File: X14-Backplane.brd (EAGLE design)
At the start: 88.9 x 139.7 mm, 34 parts, among them J2 PXC-PTSM-04-RA-1778641, J3 PXC-8-RA-1778683, J8 PXC-8-RA-1778683

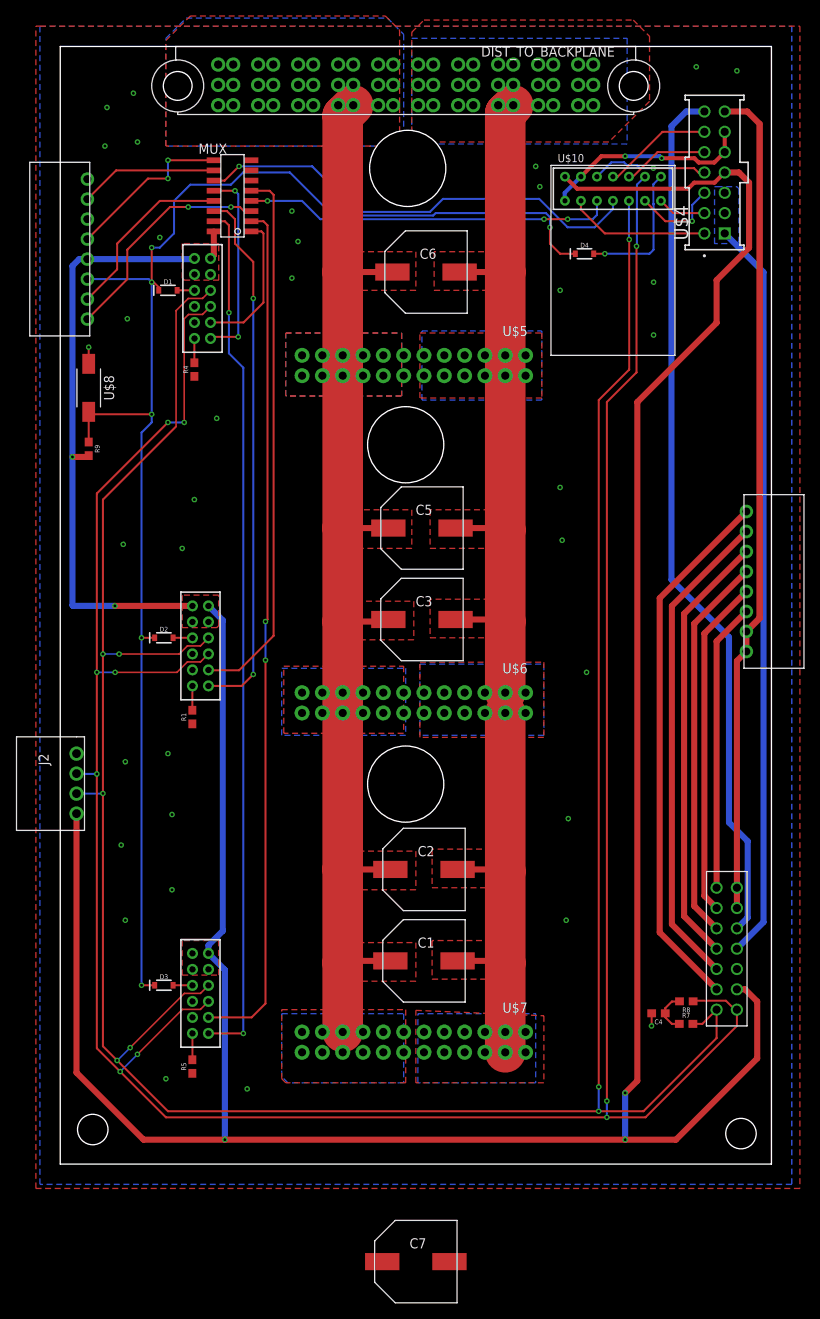
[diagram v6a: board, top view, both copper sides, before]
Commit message: todo: new cap, silkscreen
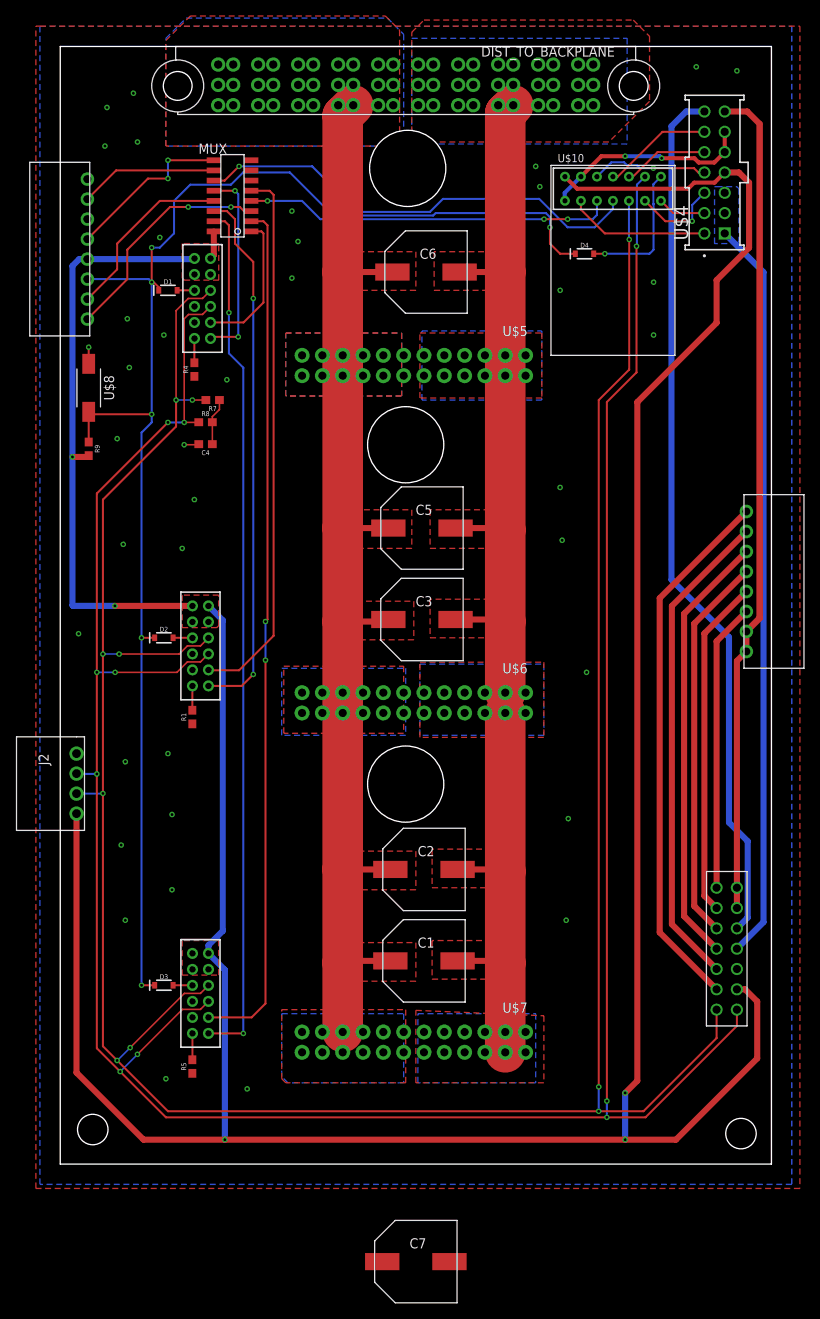
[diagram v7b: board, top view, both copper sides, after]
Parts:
- moved R7 97.9 mm to (19.1, 95.5), turned to 180 degrees
- moved R8 94.1 mm to (18.2, 92.7), turned to 0 degrees
- moved C4 90.9 mm to (18.2, 90.0)
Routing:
- net CAN_L: track 348.8 -> 344.7 mm
- net N$3: track 5.37 -> 5.88 mm
- net GND_L: track 30.0 -> 30.2 mm, vias 37 -> 41
- net CAN_H: track 340.2 -> 340.3 mm, vias 8 -> 10
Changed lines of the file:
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@@
 </autorouter>
 <elements>
-<element name="C4" library="SparkFun-Capacitors" library_urn="urn:adsk.eagle:library:510" package="0603" package3d_urn="urn:adsk.eagle:package:37414/1" value=".1uF" x="74.7776" y="18.8468" smashed="yes" rot="R180">
-<attribute name="NAME" x="74.7776" y="18.0848" size="0.6096" layer="25" font="vector" ratio="20" rot="R180" align="bottom-center"/>
-<attribute name="PROD_ID" value="CAP-00867" x="-20.4724" y="199.1868" size="1.778" layer="27" rot="R180" display="off"/>
-<attribute name="VALUE" x="74.7776" y="19.6088" size="0.6096" layer="27" font="vector" ratio="20" rot="R180" align="top-center"/>
+<element name="C4" library="SparkFun-Capacitors" library_urn="urn:adsk.eagle:library:510" package="0603" package3d_urn="urn:adsk.eagle:package:37414/1" value=".1uF" x="18.161" y="89.9922" smashed="yes" rot="R180">
+<attribute name="NAME" x="18.161" y="89.2302" size="0.6096" layer="25" font="vector" ratio="20" rot="R180" align="bottom-center"/>
+<attribute name="PROD_ID" value="CAP-00867" x="-77.089" y="270.3322" size="1.778" layer="27" rot="R180" display="off"/>
+<attribute name="VALUE" x="18.161" y="90.7542" size="0.6096" layer="27" font="vector" ratio="20" rot="R180" align="top-center"/>
 </element>
 <element name="D1" library="SparkFun-DiscreteSemi" library_urn="urn:adsk.eagle:library:514" package="SOD-323" package3d_urn="urn:adsk.eagle:package:38441/1" value="0.5A/40V/420mV" x="13.462" y="109.22" smashed="yes">
@@
 <attribute name="VALUE" x="17.272" y="12.192" size="0.6096" layer="27" font="vector" ratio="20" rot="R90" align="top-center"/>
 </element>
-<element name="R7" library="SparkFun-Resistors" library_urn="urn:adsk.eagle:library:532" package="0603" package3d_urn="urn:adsk.eagle:package:39650/1" value="60" x="78.232" y="17.526" smashed="yes">
-<attribute name="NAME" x="78.232" y="18.288" size="0.6096" layer="25" font="vector" ratio="20" align="bottom-center"/>
-<attribute name="PROD_ID" value="RES-09380" x="188.722" y="-162.814" size="1.778" layer="27" display="off"/>
-<attribute name="VALUE" x="78.232" y="16.764" size="0.6096" layer="27" font="vector" ratio="20" align="top-center"/>
-</element>
-<element name="R8" library="SparkFun-Resistors" library_urn="urn:adsk.eagle:library:532" package="0603" package3d_urn="urn:adsk.eagle:package:39650/1" value="60" x="78.2574" y="20.3454" smashed="yes" rot="R180">
-<attribute name="NAME" x="78.2574" y="19.5834" size="0.6096" layer="25" font="vector" ratio="20" rot="R180" align="bottom-center"/>
-<attribute name="PROD_ID" value="RES-09380" x="-36.0426" y="200.6854" size="1.778" layer="27" rot="R180" display="off"/>
-<attribute name="VALUE" x="78.2574" y="21.1074" size="0.6096" layer="27" font="vector" ratio="20" rot="R180" align="top-center"/>
+<element name="R7" library="SparkFun-Resistors" library_urn="urn:adsk.eagle:library:532" package="0603" package3d_urn="urn:adsk.eagle:package:39650/1" value="60" x="19.05" y="95.504" smashed="yes" rot="R180">
+<attribute name="NAME" x="19.05" y="94.742" size="0.6096" layer="25" font="vector" ratio="20" rot="R180" align="bottom-center"/>
+<attribute name="PROD_ID" value="RES-09380" x="-91.44" y="275.844" size="1.778" layer="27" rot="R180" display="off"/>
+<attribute name="VALUE" x="19.05" y="96.266" size="0.6096" layer="27" font="vector" ratio="20" rot="R180" align="top-center"/>
+</element>
+<element name="R8" library="SparkFun-Resistors" library_urn="urn:adsk.eagle:library:532" package="0603" package3d_urn="urn:adsk.eagle:package:39650/1" value="60" x="18.161" y="92.7354" smashed="yes">
+<attribute name="NAME" x="18.161" y="93.4974" size="0.6096" layer="25" font="vector" ratio="20" align="bottom-center"/>
+<attribute name="PROD_ID" value="RES-09380" x="132.461" y="-87.6046" size="1.778" layer="27" display="off"/>
+<attribute name="VALUE" x="18.161" y="91.9734" size="0.6096" layer="27" font="vector" ratio="20" align="top-center"/>
 </element>
 <element name="R9" library="SparkFun-Resistors" library_urn="urn:adsk.eagle:library:532" package="0603" package3d_urn="urn:adsk.eagle:package:39650/1" value="10k" x="3.556" y="89.408" smashed="yes" rot="R270">
@@
 <wire x1="17.78" y1="108.204" x2="16.002" y2="108.204" width="0.2032" layer="1"/>
 <wire x1="16.002" y1="108.204" x2="14.478" y2="106.68" width="0.2032" layer="1"/>
-<wire x1="14.478" y1="106.68" x2="14.478" y2="92.202" width="0.2032" layer="1"/>
+<wire x1="14.478" y1="106.68" x2="14.478" y2="95.504" width="0.2032" layer="1"/>
+<wire x1="14.478" y1="95.504" x2="14.478" y2="92.202" width="0.254" layer="1"/>
 <wire x1="2.032" y1="46.308" x2="5.3124" y2="46.308" width="0.254" layer="16"/>
 <wire x1="5.3124" y1="46.308" x2="5.334" y2="46.3296" width="0.254" layer="16"/>
 <via x="5.334" y="46.3296" extent="1-16" drill="0.35"/>
-<wire x1="82.042" y1="19.304" x2="80.264" y2="17.526" width="0.254" layer="1"/>
-<wire x1="80.264" y1="17.526" x2="79.082" y2="17.526" width="0.254" layer="1"/>
 <contactref element="U$10" pad="10"/>
 <wire x1="71.088" y1="120.409" x2="71.088" y2="115.602" width="0.254" layer="16"/>
@@
 <wire x1="67.31" y1="95.504" x2="71.12" y2="99.314" width="0.254" layer="1"/>
 <wire x1="71.12" y1="99.314" x2="71.12" y2="115.57" width="0.254" layer="1"/>
+<wire x1="18.2" y1="95.504" x2="16.51" y2="95.504" width="0.2032" layer="1"/>
+<via x="16.51" y="95.504" extent="1-16" drill="0.35"/>
+<wire x1="16.51" y1="95.504" x2="14.478" y2="95.504" width="0.2032" layer="16"/>
+<via x="14.478" y="95.504" extent="1-16" drill="0.35"/>
 </signal>
 <signal name="CAN_L">
@@
 <wire x1="4.572" y1="48.768" x2="2.072" y2="48.768" width="0.254" layer="16"/>
 <wire x1="2.072" y1="48.768" x2="2.032" y2="48.808" width="0.254" layer="16"/>
-<wire x1="84.582" y1="19.304" x2="84.328" y2="19.304" width="0.254" layer="1"/>
-<wire x1="83.2104" y1="20.4216" x2="79.1836" y2="20.4216" width="0.254" layer="1"/>
-<wire x1="79.1836" y1="20.4216" x2="79.1074" y2="20.3454" width="0.254" layer="1"/>
-<wire x1="84.328" y1="19.304" x2="83.2104" y2="20.4216" width="0.254" layer="1"/>
 <contactref element="U$10" pad="11"/>
 <wire x1="73.088" y1="123.431" x2="72.0852" y2="122.4282" width="0.254" layer="16"/>
@@
 <wire x1="72.0852" y1="122.4282" x2="72.0852" y2="114.7826" width="0.254" layer="16"/>
 <wire x1="72.0344" y1="98.9584" x2="68.326" y2="95.25" width="0.254" layer="1"/>
+<wire x1="17.311" y1="92.7354" x2="17.2856" y2="92.71" width="0.2032" layer="1"/>
+<wire x1="17.2856" y1="92.71" x2="15.494" y2="92.71" width="0.2032" layer="1"/>
 </signal>
 <signal name="5V">
@@
 <contactref element="R7" pad="1"/>
 <contactref element="C4" pad="1"/>
-<wire x1="77.4074" y1="20.3454" x2="77.382" y2="20.32" width="0.254" layer="1"/>
-<wire x1="77.382" y1="20.32" x2="76.454" y2="20.32" width="0.254" layer="1"/>
-<wire x1="76.454" y1="20.32" x2="75.6276" y2="19.4936" width="0.254" layer="1"/>
-<wire x1="75.6276" y1="19.4936" x2="75.6276" y2="18.8468" width="0.254" layer="1"/>
-<wire x1="77.382" y1="17.526" x2="76.454" y2="17.526" width="0.254" layer="1"/>
-<wire x1="76.454" y1="17.526" x2="75.6276" y2="18.3524" width="0.254" layer="1"/>
-<wire x1="75.6276" y1="18.3524" x2="75.6276" y2="18.8468" width="0.254" layer="1"/>
+<wire x1="19.011" y1="92.7354" x2="19.011" y2="92.71" width="0.2032" layer="1"/>
+<wire x1="19.011" y1="92.71" x2="19.011" y2="89.9922" width="0.2032" layer="1"/>
+<wire x1="19.9" y1="95.504" x2="19.9" y2="94.322" width="0.2032" layer="1"/>
+<wire x1="19.011" y1="93.433" x2="19.011" y2="92.7354" width="0.2032" layer="1"/>
+<wire x1="19.9" y1="94.322" x2="19.011" y2="93.433" width="0.2032" layer="1"/>
 </signal>
 <signal name="NRST_1">
@@
 <via x="15.24" y="76.962" extent="1-16" drill="0.35"/>
 <via x="16.764" y="83.058" extent="1-16" drill="0.35"/>
-<via x="19.558" y="93.218" extent="1-16" drill="0.35"/>
-<wire x1="73.9276" y1="18.8468" x2="73.9276" y2="17.2856" width="0.254" layer="1"/>
-<wire x1="73.9276" y1="17.2856" x2="73.914" y2="17.272" width="0.254" layer="1"/>
-<via x="73.914" y="17.272" extent="1-16" drill="0.35"/>
+<via x="20.828" y="98.044" extent="1-16" drill="0.35"/>
 <via x="13.462" y="51.308" extent="1-16" drill="0.35"/>
 <via x="13.97" y="43.688" extent="1-16" drill="0.35"/>
@@
 <via x="74.168" y="110.236" extent="1-16" drill="0.35"/>
 <via x="74.168" y="103.632" extent="1-16" drill="0.35"/>
+<wire x1="17.311" y1="89.9922" x2="17.2348" y2="89.916" width="0.2032" layer="1"/>
+<wire x1="17.2348" y1="89.916" x2="15.494" y2="89.916" width="0.2032" layer="1"/>
+<via x="15.494" y="89.916" extent="1-16" drill="0.35"/>
+<via x="8.636" y="99.568" extent="1-16" drill="0.35"/>
+<via x="7.112" y="90.678" extent="1-16" drill="0.35"/>
+<via x="2.286" y="66.294" extent="1-16" drill="0.35"/>
+<via x="12.954" y="103.632" extent="1-16" drill="0.35"/>
 </signal>
 <signal name="12L_GND">
